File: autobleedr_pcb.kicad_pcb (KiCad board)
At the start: 4 copper layers, 112 x 90.1 mm, 23 parts, among them J1 Barrel_Jack, J10 XT60 Connector, J11 Conn_01x02_Pin, J12 Linear Actuator Screw_Termina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, J2 Conn_01x13_Pin, J3 Conn_01x14_Pin, J4 Conn_01x08_Socket, J5 IR LED, J6 Photo Transistor, J7 Screw_Terminal_01x02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

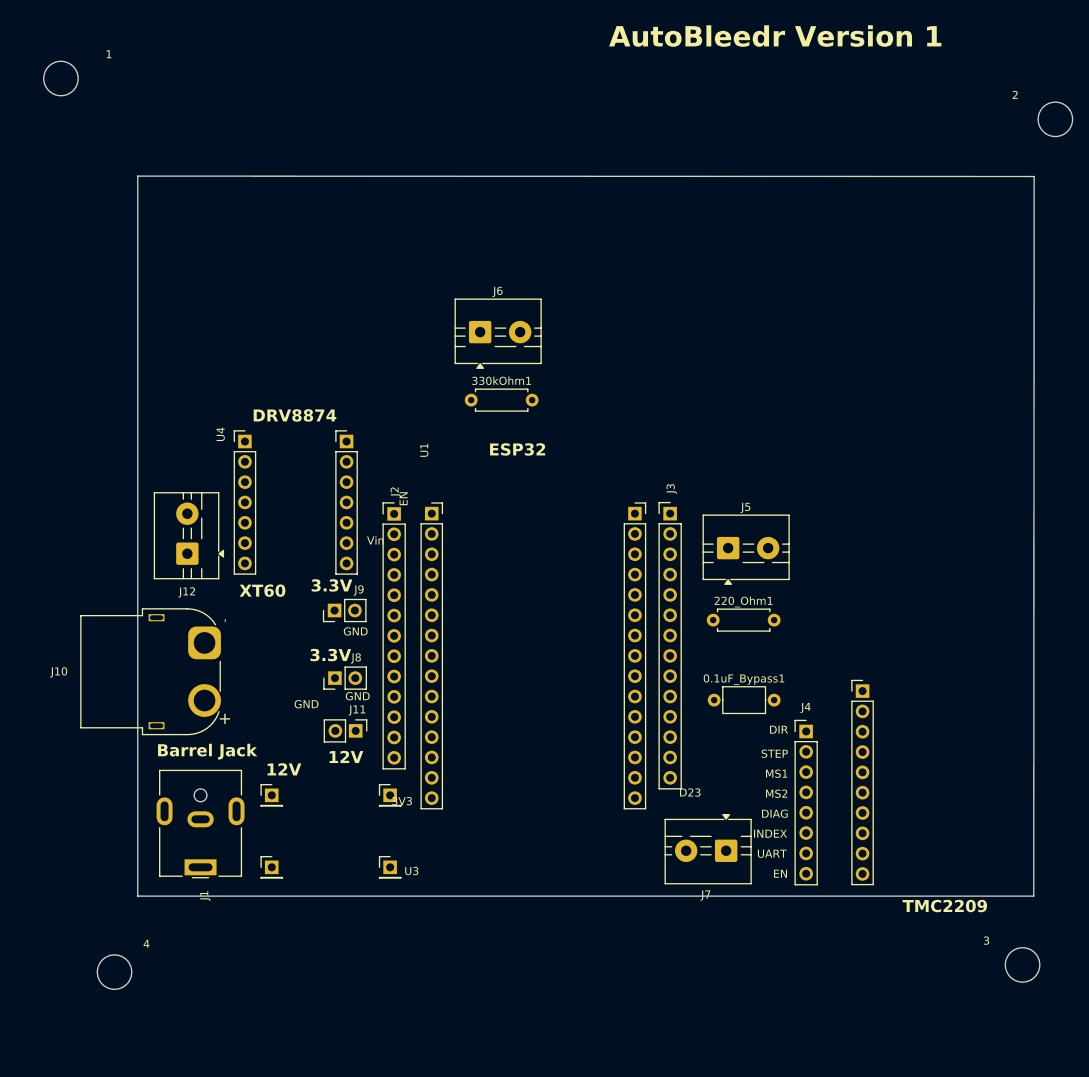
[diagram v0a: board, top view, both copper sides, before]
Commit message: Redid symbols and footprints properly
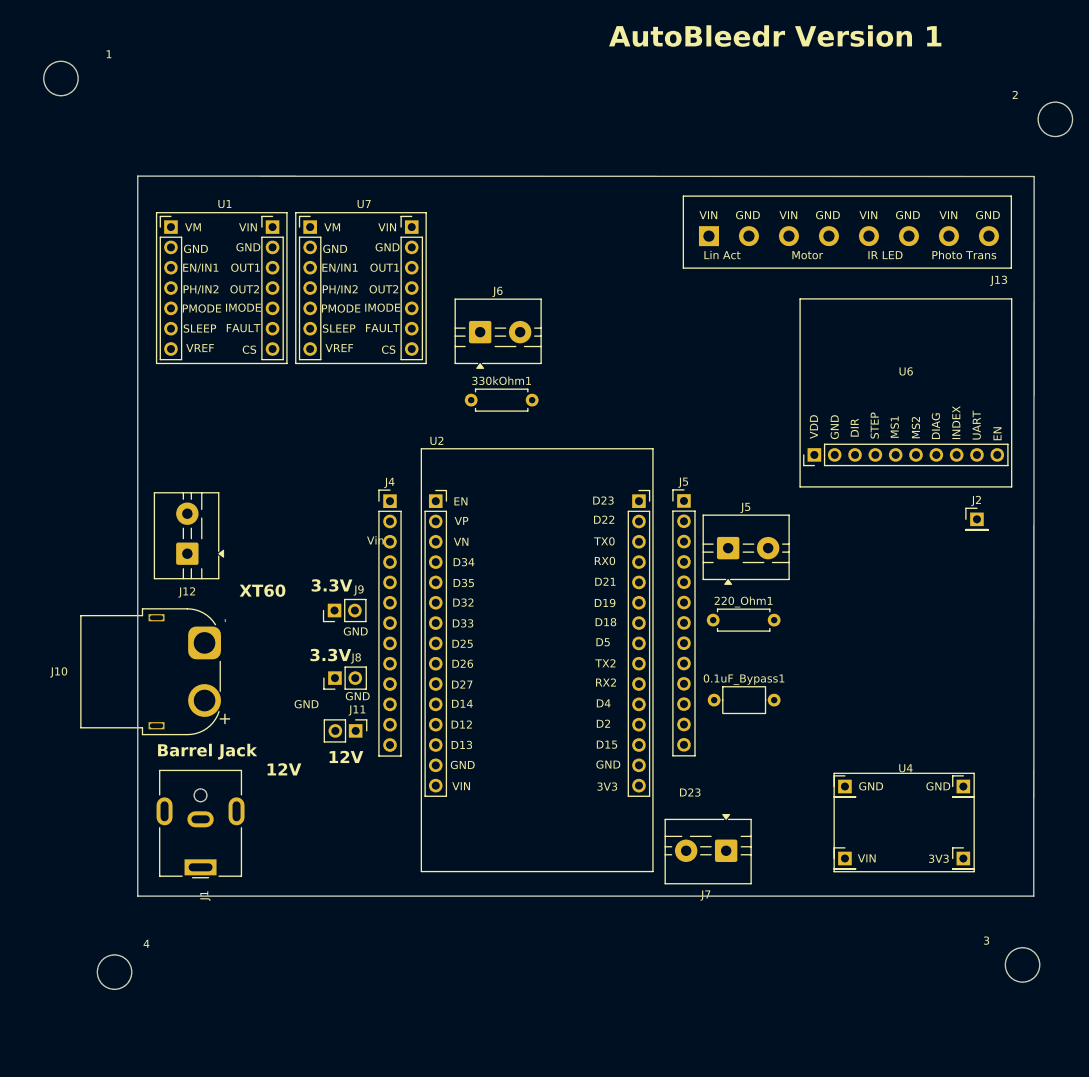
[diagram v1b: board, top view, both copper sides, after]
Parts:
- removed J3: Conn_01x14_Pin, Connector_PinHeader_2.54mm:PinHeader_1x14_P2.54mm_Vertical
- removed U3: ~, Euogeudel:Buck Converter
- added J13: Screw_Terminal_01x08, Screw_Terminal_1x8:Screw_Terminal_1x8, F.Cu at (145.4, 67.5)
- added J5: Conn_01x13_Pin, Connector_PinHeader_2.54mm:PinHeader_1x13_P2.54mm_Vertical, F.Cu at (125.0, 101.6)
- added U6: TMC2209, Capstone_Footprints:TMC2209, F.Cu at (152.7, 88.3)
- added U7: DVR8874, Capstone_Footprints:DVR8874, F.Cu at (84.7, 65.6)
- J2: value Conn_01x13_Pin -> Conn_01x01_Pin; footprint Connector_PinHeader_2.54mm:PinHeader_1x13_P2.54mm_Vertical -> Connector_PinHeader_2.54mm:PinHeader_1x01_P2.54mm_Vertical
- J4: value Conn_01x08_Socket -> Conn_01x13_Pin; footprint Connector_PinHeader_2.54mm:PinHeader_1x08_P2.54mm_Vertical -> Connector_PinHeader_2.54mm:PinHeader_1x13_P2.54mm_Vertical
- U1: value ~ -> DVR8874; footprint ESP-32:ESP-32 -> Capstone_Footprints:DVR8874
- U2: value ~ -> ESP32; footprint Adafruit:TMC2209 -> Capstone_Footprints:ESP32
- U4: value ~ -> Buck Converter; footprint Pololu:DVR8874 -> Capstone_Footprints:Buck_Converter
- moved U4 92.4 mm to (152.7, 135.6)
- moved J2 72.9 mm to (161.6, 103.9)
- moved U2 63.1 mm to (94.0, 101.6), turned to 0 degrees
- moved J4 59.5 mm to (88.2, 101.6)
- moved U1 45.8 mm to (67.3, 65.6)
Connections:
- 220_Ohm1 pad 1: D15 -> D32
- 220_Ohm1 pad 2: Net-(J5-Pin_2) -> /IR LED vin
- 330kOhm1 pad 2: D34 -> D35
- J4 pad 5: Net-(J4-Pin_5) -> D35
- J4 pad 6: Net-(J4-Pin_6) -> D32
- U1 pad 1: Net-(J2-Pin_1) -> unconnected-(U1-VM-Pad1)
- U1 pad 10: Net-(J2-Pin_10) -> unconnected-(U1-IMODE-Pad10)
- U1 pad 11: Net-(J2-Pin_11) -> /LIN ACT GND
- U1 pad 12: Net-(J2-Pin_12) -> /LIN ACT VIN
- U1 pad 13: Net-(J2-Pin_13) -> GND
- U1 pad 14: GND -> +12V
- U1 pad 2: unconnected-(J2-Pin_2-Pad2) -> GND
- U1 pad 3: unconnected-(J2-Pin_3-Pad3) -> /enable DRV
- U1 pad 4: D34 -> /linear actuator direction
- U1 pad 5: Net-(J2-Pin_5) -> GND
- U1 pad 6: Net-(J2-Pin_6) -> /enable DRV
- U1 pad 7: /linear actuator direction -> unconnected-(U1-VREF-Pad7)
- U1 pad 8: /enable DRV -> unconnected-(U1-CS-Pad8)
- U1 pad 9: Net-(J2-Pin_9) -> unconnected-(U1-FAULT-Pad9)
- U2 pad 1: +3.3V -> Net-(J4-Pin_1)
- U2 pad 10: Net-(J4-Pin_8) -> /direction ERM DRV
- U2 pad 2: GND -> Net-(J4-Pin_2)
- U2 pad 3: Net-(J4-Pin_1) -> Net-(J4-Pin_3)
- U2 pad 4: Net-(J4-Pin_2) -> Net-(J4-Pin_4)
- U2 pad 5: Net-(J4-Pin_3) -> D35
- U2 pad 6: Net-(J4-Pin_4) -> D32
- U2 pad 7: Net-(J4-Pin_5) -> Net-(J4-Pin_7)
- U2 pad 8: Net-(J4-Pin_6) -> Net-(J4-Pin_8)
- U2 pad 9: Net-(J4-Pin_7) -> /speed ERM DRV
- U4 pad 1: unconnected-(U4-VM-Pad1) -> GND
- U4 pad 2: GND -> +12V
- U4 pad 3: /enable DRV -> GND
- U4 pad 4: /linear actuator direction -> +3.3V
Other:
- board text removed: "3V3"
- board text removed: "DIAG"
- board text removed: "DIR"
- board text removed: "DRV8874"
- board text removed: "EN"
- board text removed: "ESP32"
- board text removed: "INDEX"
- board text removed: "MS1"
- board text removed: "MS2"
- board text removed: "STEP"
- board text removed: "TMC2209"
- board text removed: "UART"

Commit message: added Select Battery aka On Off Switch and power indicator LED with current limiting resistor
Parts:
- added 2200_Ohm1: R, Resistor_THT:R_Axial_DIN0207_L6.3mm_D2.5mm_P7.62mm_Horizontal, F.Cu at (100.3, 159.2)
- added D1: Power_LED, LED_THT:LED_D5.0mm_IRGrey, F.Cu at (95.2, 168.5)
- added S1: 7201SYCQE, Capstone_Footprints:7201SYCQE, F.Cu at (80.7, 147.5)
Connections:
- J1 pad 1: +12V -> BV
- J1 pad 2: GND -> BGND
- J10 pad 1: GND -> XGND
- J10 pad 2: +12V -> XV

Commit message: updated PCB
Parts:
- removed J12: Linear Actuator Screw_Terminal_01x02, TerminalBlock:TerminalBlock_MaiXu_MX126-5.0-02P_1x02_P5.00mm
- removed the J5 at (130.5, 107.5)
- removed J6: Photo Transistor, TerminalBlock:TerminalBlock_MaiXu_MX126-5.0-02P_1x02_P5.00mm
- moved D1 93.8 mm to (80.9, 75.8)
- moved J7 88.1 mm to (91.7, 66.1)
- moved J13 85.7 mm to (63.0, 91.0), turned to -90 degrees
- moved 2200_Ohm1 78.2 mm to (73.1, 85.9), turned to -90 degrees
- moved U4 77.1 mm to (76.5, 123.3), turned to 90 degrees
- moved J2 74.4 mm to (93.2, 74.6)
- moved J11 68.4 mm to (62.3, 65.5)
- moved 220_Ohm1 65.0 mm to (73.1, 82.6), turned to 90 degrees
- moved J8 59.9 mm to (67.5, 65.5)
- moved J9 49.7 mm to (76.8, 65.8)
- moved U6 44.3 mm to (110.3, 75.5)
- moved 0.1uF_Bypass1 44.2 mm to (100.6, 92.5)
- moved LinU1 39.9 mm to (70.2, 105.4), turned to 90 degrees
- moved ERMU7 23.6 mm to (76.3, 87.7), turned to 90 degrees
- moved 330kOhm1 14.5 mm to (112.5, 92.7)
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- renumbered U7 to ERMU7, U1 to LinU1
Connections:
- U6 pad 10: unconnected-(U6-EN-Pad10) -> GND
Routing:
- net Net-(J4-Pin_8): track 0.00 -> 5.95 mm
- net Net-(J4-Pin_7): track 0.00 -> 5.95 mm
- net Net-(J4-Pin_3): track 0.00 -> 5.95 mm
- net Net-(J4-Pin_1): track 0.00 -> 5.95 mm
- net D35: track 0.00 -> 5.95 mm
- net /speed ERM DRV: track 0.00 -> 5.95 mm
- net /linear actuator direction: track 0.00 -> 5.95 mm
- net /enable ERM DRV: track 0.00 -> 5.95 mm
- net /enable DRV: track 0.00 -> 5.95 mm
- net /direction ERM DRV: track 0.00 -> 5.95 mm
- net Net-(J4-Pin_4): track 0.00 -> 5.95 mm
- net Net-(J4-Pin_2): track 0.00 -> 5.95 mm
- net D32: track 0.00 -> 5.95 mm
- net Net-(J5-Pin_9): track 0.00 -> 5.64 mm
- net Net-(J5-Pin_8): track 0.00 -> 5.64 mm
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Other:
- board text removed: "Vin"

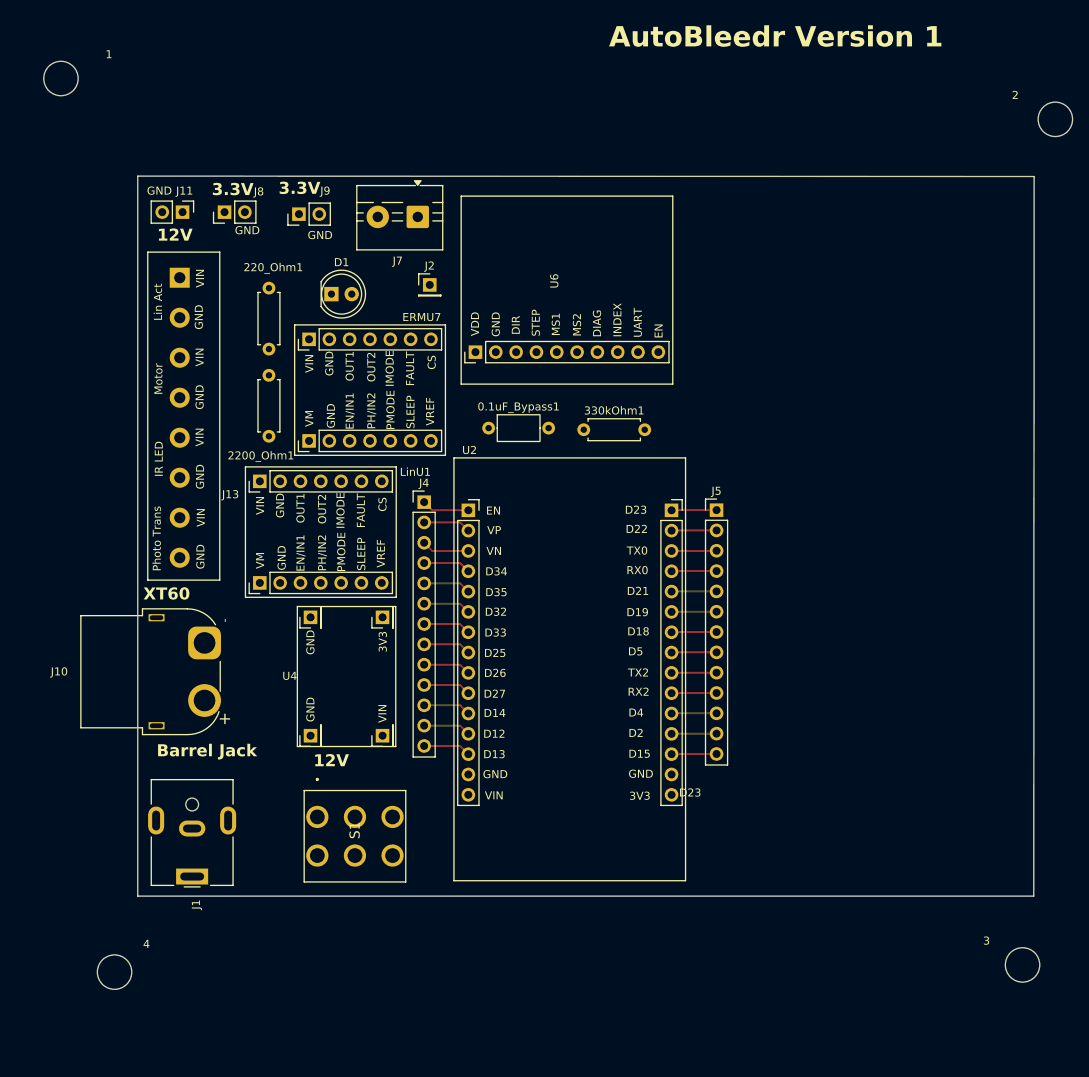
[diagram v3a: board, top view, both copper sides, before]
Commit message: added most traces
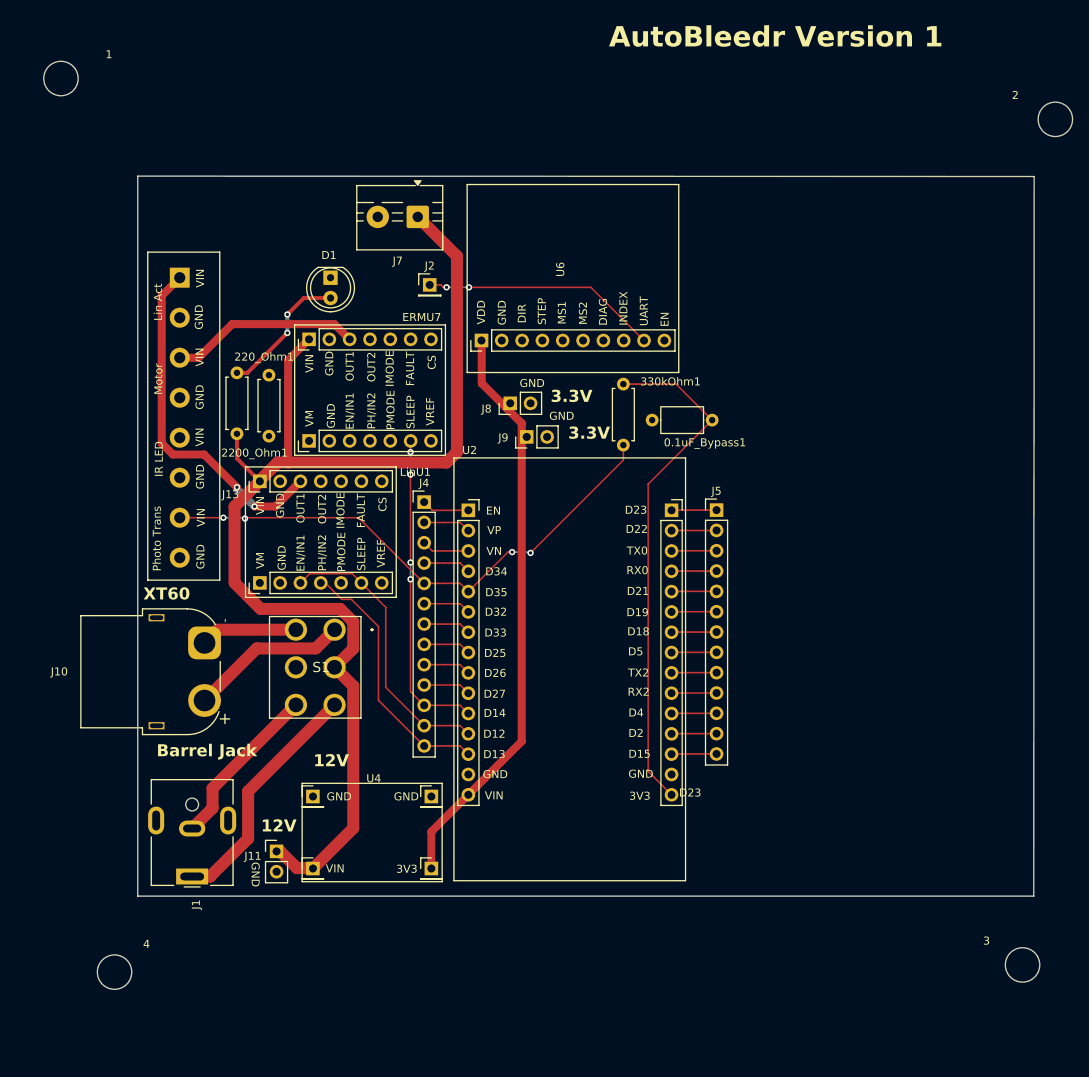
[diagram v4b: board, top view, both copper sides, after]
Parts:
- moved J11 80.8 mm to (74.0, 145.4), turned to 0 degrees
- moved J8 43.0 mm to (103.3, 89.4)
- moved J9 39.8 mm to (105.3, 93.6)
- moved 0.1uF_Bypass1 28.0 mm to (128.5, 91.5), turned to 180 degrees
- moved S1 23.5 mm to (81.3, 117.7), turned to 180 degrees
- moved U4 16.6 mm to (86.2, 136.8), turned to 0 degrees
- moved 220_Ohm1 10.9 mm to (73.1, 93.5)
- moved 330kOhm1 7.55 mm to (117.4, 87.0), turned to -90 degrees
- moved 2200_Ohm1 4.01 mm to (69.1, 85.6)
- moved D1 2.05 mm to (80.8, 73.7), turned to -90 degrees
- moved U6 1.63 mm to (111.0, 74.0)
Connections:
- U2 pad 16: +3.3V -> 3V3
- U4 pad 3: GND -> +3.3V
- U4 pad 4: +3.3V -> GND
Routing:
- net +12V: track 0.00 -> 152.4 mm
- net +3.3V: track 0.00 -> 74.5 mm
- net 3V3: track 0.00 -> 64.3 mm
- net D35: track 5.95 -> 68.1 mm, vias 0 -> 4
- net /LIN ACT VIN: track 0.00 -> 43.7 mm, vias 0 -> 2
- net /enable ERM DRV: track 5.95 -> 39.7 mm, vias 0 -> 4
- net BV: track 0.00 -> 30.1 mm
- net Net-(J2-Pin_1): track 0.00 -> 29.7 mm, vias 0 -> 2
- net /enable DRV: track 5.95 -> 35.6 mm
- net /linear actuator direction: track 5.95 -> 32.7 mm
- net /ERM vin: track 0.00 -> 23.8 mm
- net BGND: track 0.00 -> 20.8 mm
- net XV: track 0.00 -> 19.9 mm
- net Net-(D1-A): track 0.00 -> 16.9 mm, vias 0 -> 2
- net XGND: track 0.00 -> 12.1 mm

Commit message: Rerouted board and changed some gpio pins, added 3.3 led
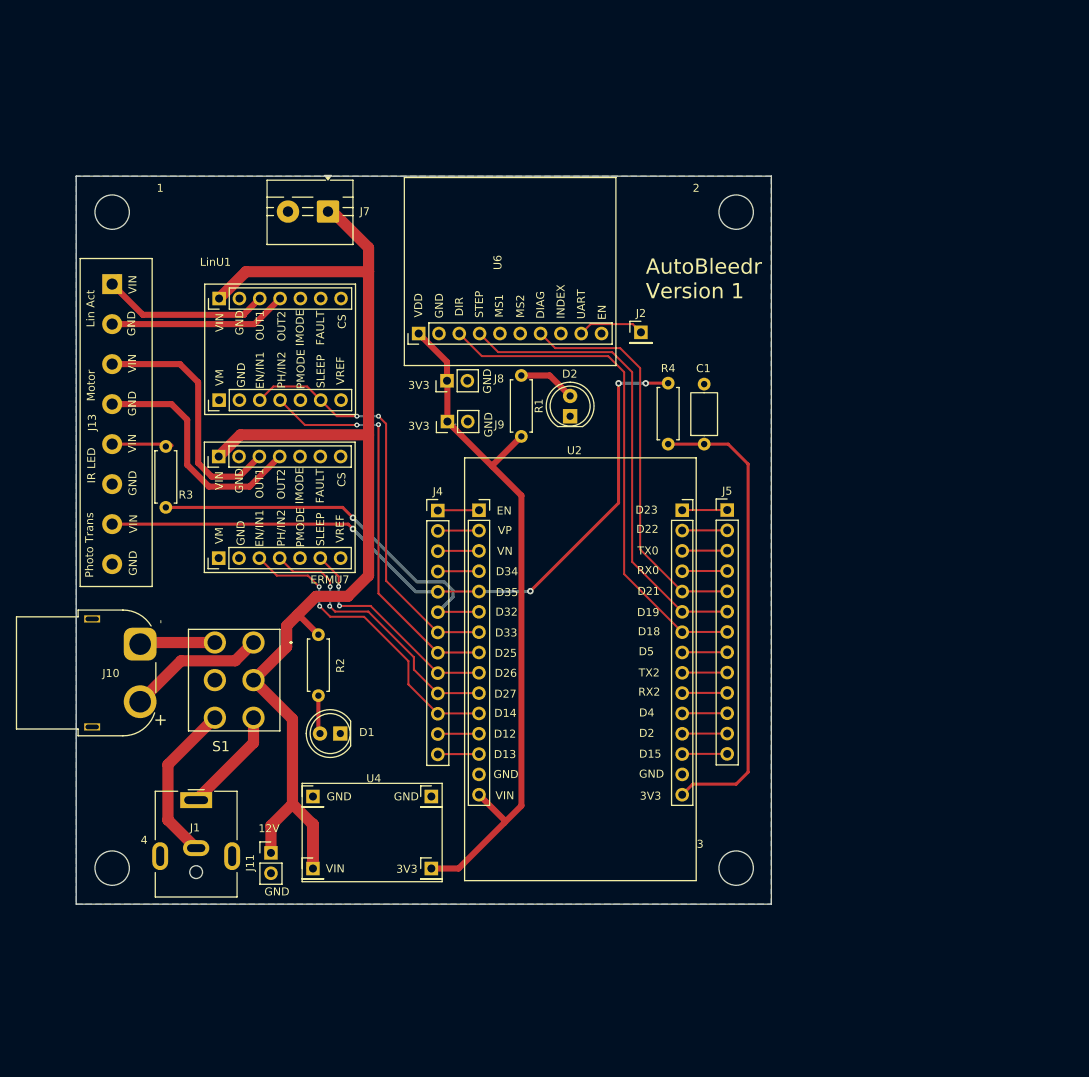
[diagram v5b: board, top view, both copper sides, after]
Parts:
- added ?: , clipboard:eeda8126-6381-443f-87cd-efa4496c9bff, F.Cu at (106.8, 111.0)
- added D2: Power_LED, LED_THT:LED_D5.0mm_IRGrey, F.Cu at (110.7, 91.0)
- added R1: 220R, Resistor_THT:R_Axial_DIN0207_L6.3mm_D2.5mm_P7.62mm_Horizontal, F.Cu at (104.6, 85.9)
- C1: renamed from 0.1uF_Bypass1; value C -> 0u1C
- R2: renamed from 2200_Ohm1; value R -> 2k2R
- R3: renamed from 220_Ohm1; value R -> 220R
- R4: renamed from 330kOhm1; value R -> 330kR
- moved D1 57.0 mm to (82.0, 130.7), turned to 180 degrees
- moved R2 41.6 mm to (79.3, 125.9), turned to 90 degrees
- moved 2 41.6 mm to (131.5, 65.5)
- moved 3 37.8 mm to (131.5, 147.5)
- moved J2 27.1 mm to (119.6, 80.5)
- moved LinU1 23.4 mm to (65.1, 82.5)
- moved ERMU7 18.5 mm to (65.0, 102.3)
- moved 1 17.9 mm to (53.5, 65.5)
- moved R3 15.7 mm to (60.2, 102.4)
- moved 4 13.0 mm to (53.5, 147.5)
- moved J7 11.2 mm to (80.5, 65.4)
- moved S1 10.3 mm to (71.2, 119.3)
- moved J9 10.1 mm to (95.4, 91.7)
- moved J1 9.56 mm to (64.0, 139.0), turned to 0 degrees
- moved R4 9.36 mm to (123.0, 94.5), turned to 90 degrees
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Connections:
- J4 pad 11: /enable ERM DRV -> /speed ERM DRV
- J4 pad 12: /enable DRV -> Net-(J4-Pin_12)
- J4 pad 13: /linear actuator direction -> Net-(J4-Pin_13)
- J4 pad 7: Net-(J4-Pin_7) -> /enable DRV
- J4 pad 8: Net-(J4-Pin_8) -> /linear actuator direction
- J4 pad 9: /speed ERM DRV -> /enable ERM DRV
- J5 pad 5: Net-(J5-Pin_5) -> /DIAG
- J5 pad 6: Net-(J5-Pin_6) -> /STEP
- J5 pad 7: Net-(J5-Pin_7) -> /DIR
- U2 pad 11: /enable ERM DRV -> /speed ERM DRV
- U2 pad 12: /enable DRV -> Net-(J4-Pin_12)
- U2 pad 13: /linear actuator direction -> Net-(J4-Pin_13)
- U2 pad 24: Net-(J5-Pin_7) -> /DIR
- U2 pad 25: Net-(J5-Pin_6) -> /STEP
- U2 pad 26: Net-(J5-Pin_5) -> /DIAG
- U2 pad 7: Net-(J4-Pin_7) -> /enable DRV
- U2 pad 8: Net-(J4-Pin_8) -> /linear actuator direction
- U2 pad 9: /speed ERM DRV -> /enable ERM DRV
- U6 pad 3: unconnected-(U6-DIR-Pad3) -> /DIR
- U6 pad 4: unconnected-(U6-STEP-Pad4) -> /STEP
- U6 pad 7: unconnected-(U6-DIAG-Pad7) -> /DIAG
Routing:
- net /DIR: track 0.00 -> 63.8 mm
- net /STEP: track 0.00 -> 59.3 mm
- net /DIAG: track 0.00 -> 50.0 mm
- net D32: track 5.95 -> 48.7 mm, vias 0 -> 1
- net /speed ERM DRV: track 5.95 -> 38.6 mm, vias 0 -> 2
- net /ERM gnd: track 0.00 -> 30.1 mm
- net /direction ERM DRV: track 5.95 -> 34.7 mm, vias 0 -> 2
- net D35: track 68.1 -> 92.4 mm
- net /LIN ACT GND: track 0.00 -> 22.3 mm
- net /LIN ACT VIN: track 43.7 -> 22.1 mm, vias 2 -> 0
- net Net-(J2-Pin_1): track 29.7 -> 8.38 mm, vias 2 -> 0
- net /linear actuator direction: track 32.7 -> 50.3 mm, vias 0 -> 2
- net BV: track 30.1 -> 13.3 mm
- net /enable DRV: track 35.6 -> 52.3 mm, vias 0 -> 2
- net +3.3V: track 74.5 -> 89.1 mm
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- added copper zone on B.Cu, net GND
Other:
- board size 112 x 90.1 mm -> 86.9 x 91 mm
- board text added: "3V3"
- board text removed: "3.3V"
- board text removed: "Barrel Jack"
- board text removed: "D23"
- board text removed: "XT60"
